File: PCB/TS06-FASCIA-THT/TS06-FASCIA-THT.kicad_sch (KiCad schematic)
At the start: 14 parts, among them J1 PH 6 SMT, SW1 SR25 6-pos, SW2 LEVER A, SW3 LEVER B, SW4 MINUS, SW5 PLUS

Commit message: PCB: TS06-FASCIA-THT, the through-hole variant, fully routed
A second build of the fascia in which the A6 divider is on show. Five axial
resistors sit on the face above the rotary's seven landing holes, and the copper
between them is bare - mask opened, ENIG gold, a solder fillet at every joint.
Everything else stays behind the panel with its front mask CLOSED, so the face
shows a drilled hole and no gold ring for those parts.

Routing: 34 tracks, no vias. The ladder is on F.Cu with the mask opened over it;
six signals run under mask on B.Cu; GND is a pour over the whole back face.

Two placement rules drove the layout and are written into the generator header:
a through-hole pad is copper on BOTH faces, so every back part must also miss the
decorative gold; and the panel parts have bodies behind the board, so R6-R8 live
in the strip below y 38.5, the only band clear of all five body keepouts.

J1's pin order is now a specification, not a routing convenience: 1 +5V, 2 GND,
3 A6, 4 A7, 5 D7, 6 D8, on BOTH builds. The old order was whatever the
surface-mount routing preferred; the through-hole board could not route to it,
and two variants of one product must not need two different cables. The
surface-mount board and the schematic are updated to match, and the shelved
routing block carries a caution that its five tails go to the old pins.

Toolchain, all of it prompted by faults found while building this board:
* tools/checkmatch.py - NEW. Compares the schematic netlist against the board
  pad by pad. Nothing did this before, which is how the two boards came to
  disagree about J1 in the first place.
* audit.py - rasterises a zone at 0.15 mm and flood-fills it, so "GND is poured"
  is a checked claim. Verified against a deliberate cut: it reports the split.
* checkpcb.py - now reads arcs and lettering on F.Cu as copper, not just lines.
  It found the plus and minus glyphs sitting 0.4 mm off the button landing pads.
* checkpcb.py, checkcopper.py - a non-greedy reach for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
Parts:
- J1: footprint TS06:TS06_JST_PH_S6B-PH-SM4-TB_Back -> TS06:TS06_JST_PH_S6B-PH-K-S_Back
- R1, R2, R3, R4, R5: footprint TS06:TS06_R_1206_HandSolder -> TS06:TS06_R_Axial_P10.16mm_Front
- R6, R7, R8: footprint TS06:TS06_R_1206_HandSolder -> TS06:TS06_R_Axial_P10.16mm_Back
- SW1: footprint TS06:TS06_Rotary_SR25_PanelMount -> TS06:TS06_Rotary_SR25_THT
- SW2, SW3: footprint TS06:TS06_MT1_Lever_PanelMount -> TS06:TS06_MT1_Lever_THT
- SW4, SW5: footprint TS06:TS06_KMD1_Button_PanelMount -> TS06:TS06_KMD1_Button_THT
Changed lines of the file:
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@@
 )
 )
-(property "Footprint" "TS06:TS06_Rotary_SR25_PanelMount"
+(property "Footprint" "TS06:TS06_Rotary_SR25_THT"
 (at 63.5 107.95 0)
 (effects
@@
 )
 )
-(property "Footprint" "TS06:TS06_R_1206_HandSolder"
+(property "Footprint" "TS06:TS06_R_Axial_P10.16mm_Front"
 (at 88.9 133.35 0)
 (effects
@@
 )
 )
-(property "Footprint" "TS06:TS06_R_1206_HandSolder"
+(property "Footprint" "TS06:TS06_R_Axial_P10.16mm_Front"
 (at 88.9 120.65 0)
 (effects
@@
 )
 )
-(property "Footprint" "TS06:TS06_R_1206_HandSolder"
+(property "Footprint" "TS06:TS06_R_Axial_P10.16mm_Front"
 (at 88.9 107.94999999999999 0)
 (effects
@@
 )
 )
-(property "Footprint" "TS06:TS06_R_1206_HandSolder"
+(property "Footprint" "TS06:TS06_R_Axial_P10.16mm_Front"
 (at 88.9 95.25 0)
 (effects
@@
 )
 )
-(property "Footprint" "TS06:TS06_R_1206_HandSolder"
+(property "Footprint" "TS06:TS06_R_Axial_P10.16mm_Front"
 (at 88.9 82.55000000000001 0)
 (effects
@@
 )
 )
-(property "Footprint" "TS06:TS06_R_1206_HandSolder"
+(property "Footprint" "TS06:TS06_R_Axial_P10.16mm_Back"
 (at 152.4 95.25 0)
 (effects
@@
 )
 )
-(property "Footprint" "TS06:TS06_MT1_Lever_PanelMount"
+(property "Footprint" "TS06:TS06_MT1_Lever_THT"
 (at 139.7 118.11 0)
 (effects
@@
 )
 )
-(property "Footprint" "TS06:TS06_R_1206_HandSolder"
+(property "Footprint" "TS06:TS06_R_Axial_P10.16mm_Back"
 (at 139.7 130.81 0)
 (effects
@@
 )
 )
-(property "Footprint" "TS06:TS06_MT1_Lever_PanelMount"
+(property "Footprint" "TS06:TS06_MT1_Lever_THT"
 (at 165.1 118.11 0)
 (effects
@@
 )
 )
-(property "Footprint" "TS06:TS06_R_1206_HandSolder"
+(property "Footprint" "TS06:TS06_R_Axial_P10.16mm_Back"
 (at 165.1 130.81 0)
 (effects
@@
 )
 )
-(property "Footprint" "TS06:TS06_KMD1_Button_PanelMount"
+(property "Footprint" "TS06:TS06_KMD1_Button_THT"
 (at 201.93 107.95 0)
 (effects
@@
 )
 )
-(property "Footprint" "TS06:TS06_KMD1_Button_PanelMount"
+(property "Footprint" "TS06:TS06_KMD1_Button_THT"
 (at 227.33 107.95 0)
 (effects
@@
 )
 )
-(property "Footprint" "TS06:TS06_JST_PH_S6B-PH-SM4-TB_Back"
+(property "Footprint" "TS06:TS06_JST_PH_S6B-PH-K-S_Back"
 (at 238.76 80.01 0)
 (effects

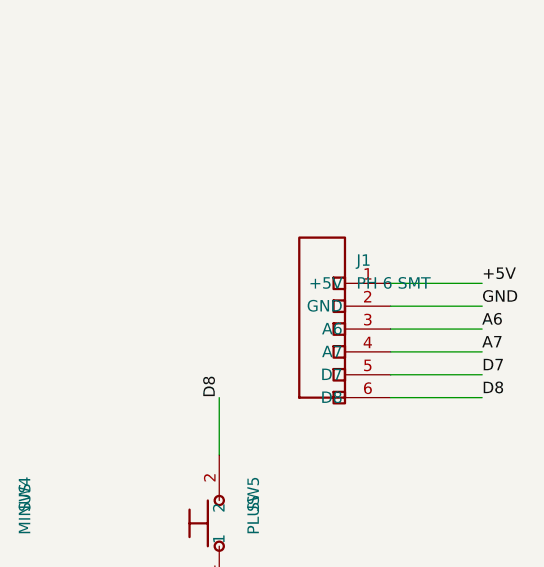
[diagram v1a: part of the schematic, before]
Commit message: sch: the panel connector symbol is JST-PH, not XH
The footprint, the buy list and the physical part have been PH 2.0 mm since the
connector was chosen. Only the symbol name still said XH, which is exactly the
kind of stale label that gets ordered against.

Co-Authored-By: Claude Opus 5 <noreply@anthropic.com>
Claude-Session: https://claude.ai/code/session_01Wbajb7CU1SV8ZUPn3KkB8i
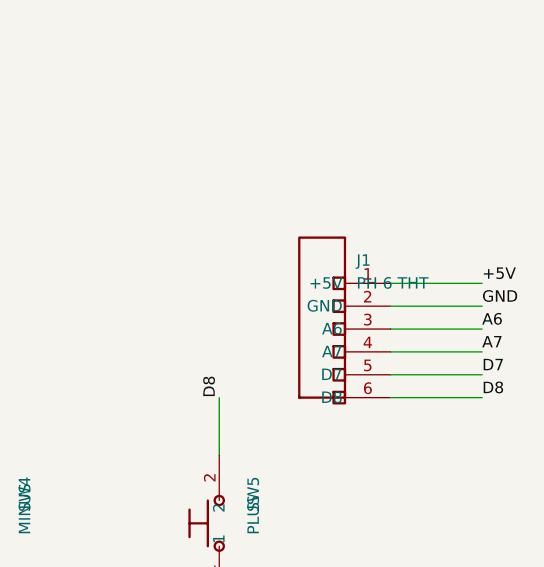
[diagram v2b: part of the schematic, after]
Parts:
- removed J1: PH 6 SMT, TS06:TS06_JST_PH_S6B-PH-K-S_Back, symbol TS06:Conn_JST_XH_6
- added J1: PH 6 THT, TS06:TS06_JST_PH_S6B-PH-K-S_Back, symbol TS06:Conn_JST_PH_6
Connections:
- net +5V: now also J1.1 (+5V)
- net A6: now also J1.3 (A6)
- net A7: now also J1.4 (A7)
- net D7: now also J1.5 (D7)
- net D8: now also J1.6 (D8)
- net GND: now also J1.2 (GND)
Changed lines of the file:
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@@
 )
 (symbol
-(lib_id "TS06:Conn_JST_XH_6")
+(lib_id "TS06:Conn_JST_PH_6")
 (at 238.76 80.01 0)
 (unit 1)
@@
 )
 )
-(property "Value" "PH 6 SMT"
+(property "Value" "PH 6 THT"
 (at 242.57 81.28 0)
 (effects
